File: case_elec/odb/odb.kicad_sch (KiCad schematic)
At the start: 9 parts, among them J1 Screw_Terminal_01x02, J2 Conn_02x07_Top_Bottom, SW1 SW_SPST, SW2 SW_SPST, U1 REYAX RYLR896, U2 BNO055, U3 MPL3115A, U4 Ultimate_GPS, U5 Teensy3.5

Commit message: amélioration route sw
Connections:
- net +5V: no longer SW2.2 (B)
- net at J1.1 (Pin_1), SW1.1 (A): now also SW2.2 (B)
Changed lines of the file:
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@@
   (junction (at 144.78 34.29) (diameter 0) (color 0 0 0 0)
   )
+  (junction (at 58.42 81.28) (diameter 0) (color 0 0 0 0)
+  )
   (junction (at 72.39 81.28) (diameter 0) (color 0 0 0 0)
   )
@@
     (stroke (width 0) (type default) (color 0 0 0 0))
   )
-  (wire (pts (xy 59.69 81.28) (xy 57.15 81.28))
+  (wire (pts (xy 59.69 81.28) (xy 58.42 81.28))
     (stroke (width 0) (type default) (color 0 0 0 0))
   )
@@
     (stroke (width 0) (type default) (color 0 0 0 0))
   )
-  (polyline (pts (xy 20.32 115.57) (xy 92.71 115.57))
+  (polyline (pts (xy 20.32 115.57) (xy 96.52 115.57))
     (stroke (width 0) (type default) (color 0 0 0 0))
   )
@@
     (stroke (width 0) (type default) (color 0 0 0 0))
   )
-  (polyline (pts (xy 92.71 115.57) (xy 92.71 152.4))
+  (polyline (pts (xy 96.52 115.57) (xy 96.52 152.4))
     (stroke (width 0) (type default) (color 0 0 0 0))
   )
@@
     (stroke (width 0) (type default) (color 0 0 0 0))
   )
-  (wire (pts (xy 77.47 142.24) (xy 95.25 142.24))
-    (stroke (width 0) (type default) (color 0 0 0 0))
-  )
   (wire (pts (xy 167.64 158.75) (xy 163.83 158.75))
     (stroke (width 0) (type default) (color 0 0 0 0))
@@
     (stroke (width 0) (type default) (color 0 0 0 0))
   )
+  (wire (pts (xy 58.42 81.28) (xy 58.42 113.03))
+    (stroke (width 0) (type default) (color 0 0 0 0))
+  )
   (wire (pts (xy 129.54 39.37) (xy 151.13 39.37))
     (stroke (width 0) (type default) (color 0 0 0 0))
   )
+  (wire (pts (xy 77.47 142.24) (xy 99.06 142.24))
+    (stroke (width 0) (type default) (color 0 0 0 0))
+  )
   (wire (pts (xy 107.95 83.82) (xy 99.06 83.82))
     (stroke (width 0) (type default) (color 0 0 0 0))
@@
     (stroke (width 0) (type default) (color 0 0 0 0))
   )
-  (wire (pts (xy 95.25 128.27) (xy 95.25 129.54))
-    (stroke (width 0) (type default) (color 0 0 0 0))
-  )
   (bus (pts (xy 170.18 171.45) (xy 170.18 168.91))
     (stroke (width 0) (type default) (color 0 0 0 0))
@@
     (stroke (width 0) (type default) (color 0 0 0 0))
   )
-  (polyline (pts (xy 92.71 152.4) (xy 20.32 152.4))
+  (polyline (pts (xy 96.52 152.4) (xy 20.32 152.4))
     (stroke (width 0) (type default) (color 0 0 0 0))
   )
@@
     (stroke (width 0) (type default) (color 0 0 0 0))
   )
-  (wire (pts (xy 91.44 129.54) (xy 95.25 129.54))
+  (wire (pts (xy 91.44 129.54) (xy 92.71 129.54))
     (stroke (width 0) (type default) (color 0 0 0 0))
   )
@@
     (stroke (width 0) (type default) (color 0 0 0 0))
   )
-  (wire (pts (xy 95.25 142.24) (xy 95.25 143.51))
+  (wire (pts (xy 99.06 142.24) (xy 99.06 143.51))
     (stroke (width 0) (type default) (color 0 0 0 0))
   )
@@
     (stroke (width 0) (type default) (color 0 0 0 0))
   )
+  (wire (pts (xy 58.42 81.28) (xy 57.15 81.28))
+    (stroke (width 0) (type default) (color 0 0 0 0))
+  )
   (wire (pts (xy 107.95 54.61) (xy 151.13 54.61))
     (stroke (width 0) (type default) (color 0 0 0 0))
@@
     (stroke (width 0) (type default) (color 0 0 0 0))
   )
+  (wire (pts (xy 58.42 113.03) (xy 92.71 113.03))
+    (stroke (width 0) (type default) (color 0 0 0 0))
+  )
   (wire (pts (xy 151.13 161.29) (xy 147.32 161.29))
     (stroke (width 0) (type default) (color 0 0 0 0))
@@
   )
   (wire (pts (xy 102.87 93.98) (xy 99.06 93.98))
+    (stroke (width 0) (type default) (color 0 0 0 0))
+  )
+  (wire (pts (xy 92.71 113.03) (xy 92.71 129.54))
     (stroke (width 0) (type default) (color 0 0 0 0))
   )
@@
     (pin "~")
   )
-  (symbol (lib_id "power:GND") (at 95.25 143.51 0) (unit 1)
-    (in_bom yes) (on_board yes)
-    (property "Reference" "#PWR04" (id 0) (at 95.25 149.86 0)
-      (effects (font (size 1.27 1.27)) hide)
-    )
-    (property "Value" "GND" (id 1) (at 95.25 148.59 0))
-    (property "Footprint" "" (id 2) (at 95.25 143.51 0)
-      (effects (font (size 1.27 1.27)) hide)
-    )
-    (property "Datasheet" "" (id 3) (at 95.25 143.51 0)
+  (symbol (lib_id "power:GND") (at 99.06 143.51 0) (unit 1)
+    (in_bom yes) (on_board yes)
+    (property "Reference" "#PWR04" (id 0) (at 99.06 149.86 0)
+      (effects (font (size 1.27 1.27)) hide)
+    )
+    (property "Value" "GND" (id 1) (at 99.06 148.59 0))
+    (property "Footprint" "" (id 2) (at 99.06 143.51 0)
+      (effects (font (size 1.27 1.27)) hide)
+    )
+    (property "Datasheet" "" (id 3) (at 99.06 143.51 0)
       (effects (font (size 1.27 1.27)) hide)
     )
@@
     (pin "6")
   )
-  (symbol (lib_id "power:+5V") (at 95.25 128.27 0) (unit 1)
-    (in_bom yes) (on_board yes)
-    (property "Reference" "#PWR03" (id 0) (at 95.25 132.08 0)
-      (effects (font (size 1.27 1.27)) hide)
-    )
-    (property "Value" "+5V" (id 1) (at 95.25 123.19 0))
-    (property "Footprint" "" (id 2) (at 95.25 128.27 0)
-      (effects (font (size 1.27 1.27)) hide)
-    )
-    (property "Datasheet" "" (id 3) (at 95.25 128.27 0)
-      (effects (font (size 1.27 1.27)) hide)
-    )
-    (pin "1")
-  )
   (symbol (lib_id "power:+5V") (at 72.39 82.55 180) (unit 1)
     (in_bom yes) (on_board yes) (fields_autoplaced)
@@
       (reference "#PWR02") (unit 1) (value "+5V") (footprint "")
     )
-    (path "/bacfcaea-5c0b-42ab-980e-cb8f47a6819e"
-      (reference "#PWR03") (unit 1) (value "+5V") (footprint "")
-    )
     (path "/7e28eb0b-eb99-4229-b4b8-2afb2f4b8e69"

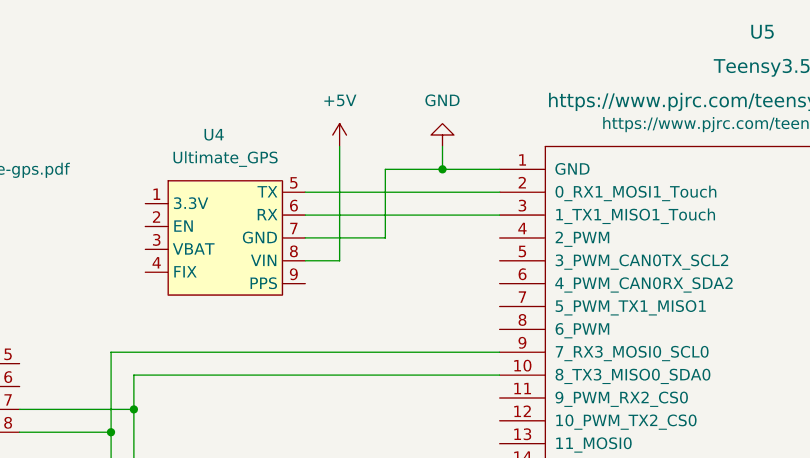
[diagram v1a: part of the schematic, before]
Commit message: Nouveau mapping perçage + gerber
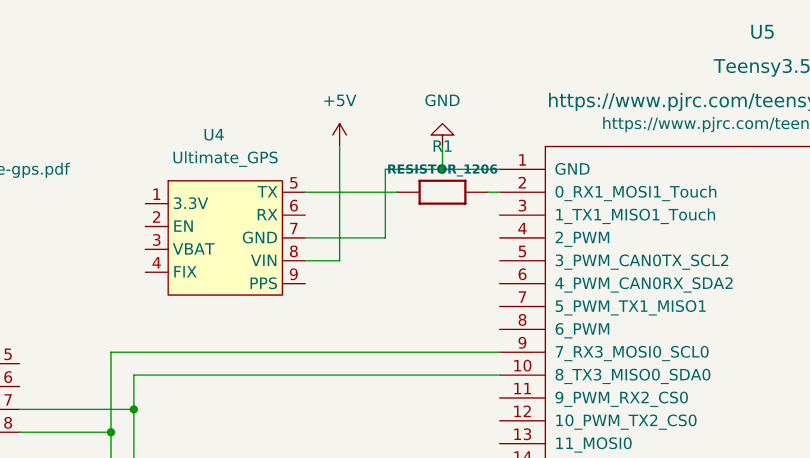
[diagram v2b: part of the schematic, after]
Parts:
- added R1: RESISTOR_1206, Resistor_SMD:R_1206_3216Metric_Pad1.30x1.75mm_HandSolder, symbol odb-eagle-import:RESISTOR_1206
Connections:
- net at U5.2 (0_RX1_MOSI1_Touch): now also R1.2; no longer U4.5 (TX)
- net at U5.3 (1_TX1_MISO1_Touch): no longer U4.6 (RX)
- new net: R1.1, U4.5 (TX)
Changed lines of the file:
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@@
+    (stroke (width 0) (type default) (color 0 0 0 0))
+  )
+  (wire (pts (xy 149.86 36.83) (xy 151.13 36.83))
+    (stroke (width 0) (type default) (color 0 0 0 0))
+  )
+  (wire (pts (xy 129.54 36.83) (xy 139.7 36.83))
     (stroke (width 0) (type default) (color 0 0 0 0))
   )
@@
     (stroke (width 0) (type default) (color 0 0 0 0))
   )
-  (wire (pts (xy 129.54 39.37) (xy 151.13 39.37))
-    (stroke (width 0) (type default) (color 0 0 0 0))
-  )
   (wire (pts (xy 77.47 142.24) (xy 99.06 142.24))
     (stroke (width 0) (type default) (color 0 0 0 0))
@@
   )
   (polyline (pts (xy 96.52 152.4) (xy 20.32 152.4))
-    (stroke (width 0) (type default) (color 0 0 0 0))
-  )
-  (wire (pts (xy 129.54 36.83) (xy 151.13 36.83))
     (stroke (width 0) (type default) (color 0 0 0 0))
   )
@@
     (pin "2")
   )
+  (symbol (lib_id "odb-eagle-import:RESISTOR_1206") (at 144.78 36.83 0) (unit 1)
+    (in_bom yes) (on_board yes) (fields_autoplaced)
+    (property "Reference" "R1" (id 0) (at 144.78 31.75 0))
+    (property "Value" "RESISTOR_1206" (id 1) (at 144.78 34.29 0)
+      (effects (font (size 1.016 1.016) bold))
+    )
+    (property "Footprint" "Resistor_SMD:R_1206_3216Metric_Pad1.30x1.75mm_HandSolder" (id 2) (at 144.78 36.83 0)
+      (effects (font (size 1.27 1.27)) hide)
+    )
+    (property "Datasheet" "" (id 3) (at 144.78 36.83 0)
+      (effects (font (size 1.27 1.27)) hide)
+    )
+    (pin "1")
+    (pin "2")
+  )
   (symbol (lib_id "reyax_rylr896:REYAX RYLR896") (at 59.69 135.89 0) (mirror y) (unit 1)
     (in_bom yes) (on_board yes)
@@
       (reference "J2") (unit 1) (value "Conn_02x07_Top_Bottom") (footprint "Connector_Molex:Molex_Nano-Fit_105310-xx14_2x07_P2.50mm_Vertical")
     )
+    (path "/92122d1f-5730-4015-aa36-a6febc7e4df1"
+      (reference "R1") (unit 1) (value "RESISTOR_1206") (footprint "Resistor_SMD:R_1206_3216Metric_Pad1.30x1.75mm_HandSolder")
+    )
     (path "/9077b56f-c102-47b4-9a60-c432e96c7e85"

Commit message: Suppression de la deuxième smd + modification sur le schema
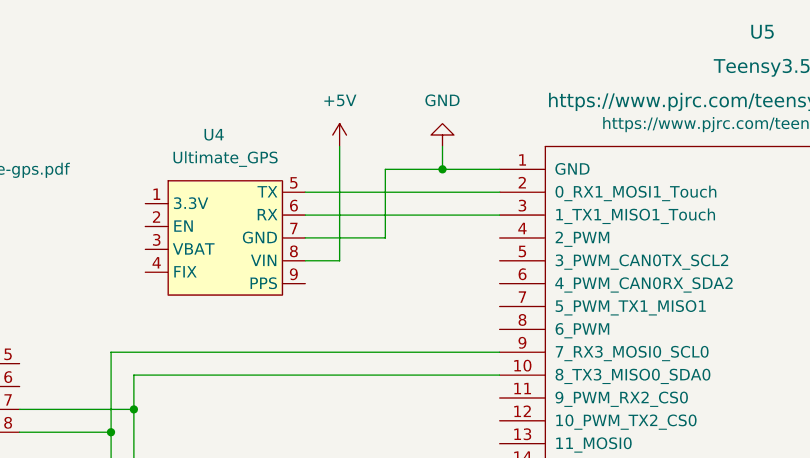
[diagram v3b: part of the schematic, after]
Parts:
- removed R1: RESISTOR_1206, Resistor_SMD:R_1206_3216Metric_Pad1.30x1.75mm_HandSolder, symbol odb-eagle-import:RESISTOR_1206
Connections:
- net at U5.2 (0_RX1_MOSI1_Touch): now also U4.5 (TX)
- net at U5.3 (1_TX1_MISO1_Touch): now also U4.6 (RX)
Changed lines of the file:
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@@
     (stroke (width 0) (type default) (color 0 0 0 0))
   )
-  (wire (pts (xy 149.86 36.83) (xy 151.13 36.83))
-    (stroke (width 0) (type default) (color 0 0 0 0))
-  )
-  (wire (pts (xy 129.54 36.83) (xy 139.7 36.83))
+  (wire (pts (xy 129.54 36.83) (xy 151.13 36.83))
     (stroke (width 0) (type default) (color 0 0 0 0))
   )
@@
   )
   (wire (pts (xy 58.42 81.28) (xy 58.42 113.03))
+    (stroke (width 0) (type default) (color 0 0 0 0))
+  )
+  (wire (pts (xy 129.54 39.37) (xy 151.13 39.37))
     (stroke (width 0) (type default) (color 0 0 0 0))
   )
@@
     (pin "2")
   )
-  (symbol (lib_id "odb-eagle-import:RESISTOR_1206") (at 144.78 36.83 0) (unit 1)
-    (in_bom yes) (on_board yes) (fields_autoplaced)
-    (property "Reference" "R1" (id 0) (at 144.78 31.75 0))
-    (property "Value" "RESISTOR_1206" (id 1) (at 144.78 34.29 0)
-      (effects (font (size 1.016 1.016) bold))
-    )
-    (property "Footprint" "Resistor_SMD:R_1206_3216Metric_Pad1.30x1.75mm_HandSolder" (id 2) (at 144.78 36.83 0)
-      (effects (font (size 1.27 1.27)) hide)
-    )
-    (property "Datasheet" "" (id 3) (at 144.78 36.83 0)
-      (effects (font (size 1.27 1.27)) hide)
-    )
-    (pin "1")
-    (pin "2")
-  )
   (symbol (lib_id "reyax_rylr896:REYAX RYLR896") (at 59.69 135.89 0) (mirror y) (unit 1)
     (in_bom yes) (on_board yes)
@@
       (reference "J2") (unit 1) (value "Conn_02x07_Top_Bottom") (footprint "Connector_Molex:Molex_Nano-Fit_105310-xx14_2x07_P2.50mm_Vertical")
     )
-    (path "/92122d1f-5730-4015-aa36-a6febc7e4df1"
-      (reference "R1") (unit 1) (value "RESISTOR_1206") (footprint "Resistor_SMD:R_1206_3216Metric_Pad1.30x1.75mm_HandSolder")
-    )
     (path "/9077b56f-c102-47b4-9a60-c432e96c7e85"

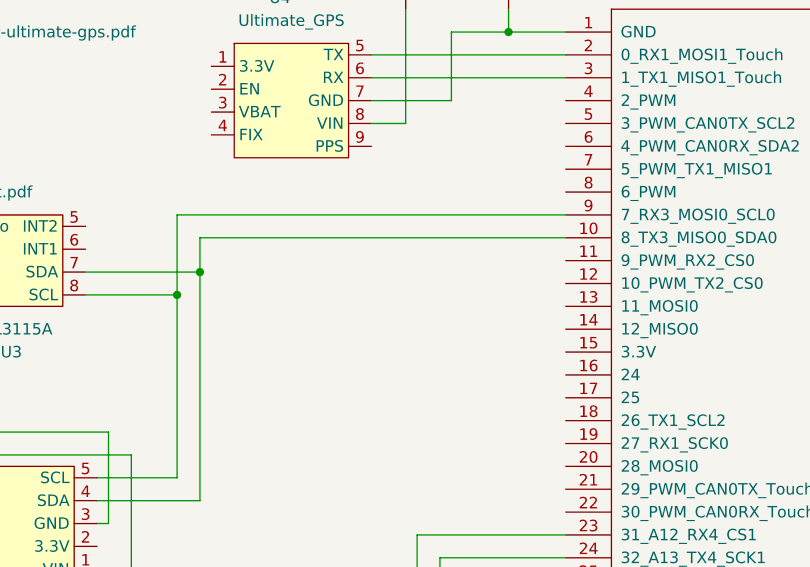
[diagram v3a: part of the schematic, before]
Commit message: Amélioration du code + fsm multitache
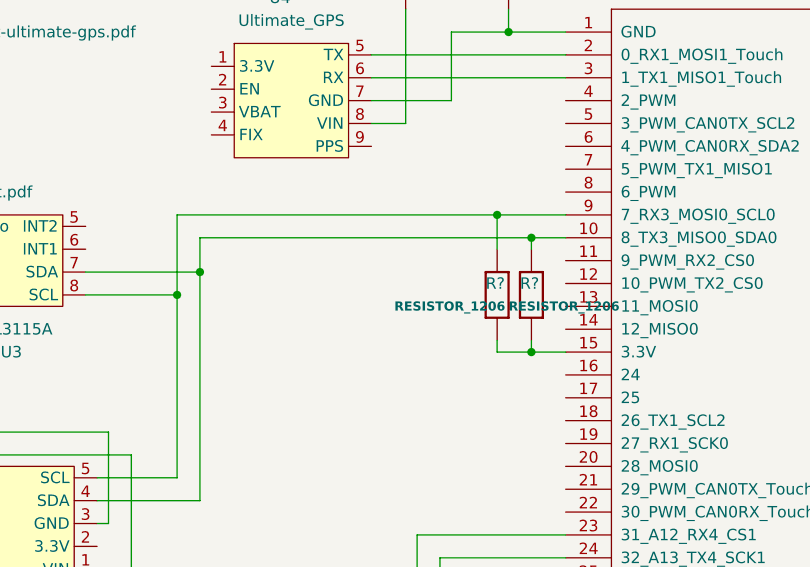
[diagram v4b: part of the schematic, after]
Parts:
- added R? (x2): RESISTOR_1206, odb:_1206, symbol odb-eagle-import:RESISTOR_1206
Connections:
- net at U2.4 (SDA), U3.7 (SDA), U5.10 (8_TX3_MISO0_SDA0): now also R?.2
- net at U2.5 (SCL), U3.8 (SCL), U5.9 (7_RX3_MOSI0_SCL0): now also R?.2
- net at U5.15 (3.3V): now also R?.1, R?.1
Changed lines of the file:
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@@
   (junction (at 76.2 78.74) (diameter 0) (color 0 0 0 0)
   )
+  (junction (at 147.32 69.85) (diameter 0) (color 0 0 0 0)
+  )
   (junction (at 170.18 153.67) (diameter 0) (color 0 0 0 0)
   )
@@
   (junction (at 58.42 81.28) (diameter 0) (color 0 0 0 0)
   )
+  (junction (at 147.32 57.15) (diameter 0) (color 0 0 0 0)
+  )
   (junction (at 72.39 81.28) (diameter 0) (color 0 0 0 0)
   )
@@
   (junction (at 110.49 60.96) (diameter 0) (color 0 0 0 0)
   )
+  (junction (at 143.51 54.61) (diameter 0) (color 0 0 0 0)
+  )
   (bus_entry (at 167.64 158.75) (size 2.54 -2.54)
     (stroke (width 0) (type default) (color 0 0 0 0))
@@
     (stroke (width 0) (type default) (color 0 0 0 0))
   )
+  (wire (pts (xy 143.51 69.85) (xy 147.32 69.85))
+    (stroke (width 0) (type default) (color 0 0 0 0))
+  )
   (wire (pts (xy 151.13 173.99) (xy 147.32 173.99))
     (stroke (width 0) (type default) (color 0 0 0 0))
@@
     (stroke (width 0) (type default) (color 0 0 0 0))
   )
+  (wire (pts (xy 143.51 68.58) (xy 143.51 69.85))
+    (stroke (width 0) (type default) (color 0 0 0 0))
+  )
   (wire (pts (xy 167.64 158.75) (xy 163.83 158.75))
     (stroke (width 0) (type default) (color 0 0 0 0))
@@
     (stroke (width 0) (type default) (color 0 0 0 0))
   )
+  (wire (pts (xy 147.32 68.58) (xy 147.32 69.85))
+    (stroke (width 0) (type default) (color 0 0 0 0))
+  )
   (bus (pts (xy 144.78 163.83) (xy 144.78 161.29))
     (stroke (width 0) (type default) (color 0 0 0 0))
@@
     (stroke (width 0) (type default) (color 0 0 0 0))
   )
+  (wire (pts (xy 147.32 69.85) (xy 151.13 69.85))
+    (stroke (width 0) (type default) (color 0 0 0 0))
+  )
   (wire (pts (xy 167.64 161.29) (xy 163.83 161.29))
     (stroke (width 0) (type default) (color 0 0 0 0))
@@
     (stroke (width 0) (type default) (color 0 0 0 0))
   )
+  (wire (pts (xy 147.32 57.15) (xy 151.13 57.15))
+    (stroke (width 0) (type default) (color 0 0 0 0))
+  )
   (wire (pts (xy 151.13 163.83) (xy 147.32 163.83))
     (stroke (width 0) (type default) (color 0 0 0 0))
@@
     (stroke (width 0) (type default) (color 0 0 0 0))
   )
-  (wire (pts (xy 107.95 54.61) (xy 151.13 54.61))
+  (wire (pts (xy 107.95 54.61) (xy 143.51 54.61))
     (stroke (width 0) (type default) (color 0 0 0 0))
   )
@@
     (stroke (width 0) (type default) (color 0 0 0 0))
   )
-  (wire (pts (xy 110.49 57.15) (xy 151.13 57.15))
+  (wire (pts (xy 110.49 57.15) (xy 147.32 57.15))
     (stroke (width 0) (type default) (color 0 0 0 0))
   )
@@
     (stroke (width 0) (type default) (color 0 0 0 0))
   )
+  (wire (pts (xy 143.51 54.61) (xy 143.51 58.42))
+    (stroke (width 0) (type default) (color 0 0 0 0))
+  )
   (wire (pts (xy 69.85 81.28) (xy 72.39 81.28))
     (stroke (width 0) (type default) (color 0 0 0 0))
@@
     (stroke (width 0) (type default) (color 0 0 0 0))
   )
+  (wire (pts (xy 143.51 54.61) (xy 151.13 54.61))
+    (stroke (width 0) (type default) (color 0 0 0 0))
+  )
   (wire (pts (xy 138.43 34.29) (xy 144.78 34.29))
     (stroke (width 0) (type default) (color 0 0 0 0))
@@
   )
   (bus (pts (xy 144.78 128.27) (xy 144.78 130.81))
+    (stroke (width 0) (type default) (color 0 0 0 0))
+  )
+  (wire (pts (xy 147.32 57.15) (xy 147.32 58.42))
     (stroke (width 0) (type default) (color 0 0 0 0))
   )
@@
     )
     (pin "1")
+  )
+  (symbol (lib_id "odb-eagle-import:RESISTOR_1206") (at 143.51 63.5 90) (unit 1)
+    (in_bom yes) (on_board yes)
+    (property "Reference" "R?" (id 0) (at 142.24 62.23 90)
+      (effects (font (size 1.27 1.27)) (justify right))
+    )
+    (property "Value" "RESISTOR_1206" (id 1) (at 132.08 64.77 90)
+      (effects (font (size 1.016 1.016) bold) (justify right))
+    )
+    (property "Footprint" "odb:_1206" (id 2) (at 143.51 63.5 0)
+      (effects (font (size 1.27 1.27)) hide)
+    )
+    (property "Datasheet" "" (id 3) (at 143.51 63.5 0)
+      (effects (font (size 1.27 1.27)) hide)
+    )
+    (pin "1")
+    (pin "2")
   )
   (symbol (lib_id "power:GND") (at 144.78 31.75 180) (unit 1)
@@
     (pin "6")
   )
+  (symbol (lib_id "odb-eagle-import:RESISTOR_1206") (at 147.32 63.5 90) (unit 1)
+    (in_bom yes) (on_board yes)
+    (property "Reference" "R?" (id 0) (at 146.05 62.23 90)
+      (effects (font (size 1.27 1.27)) (justify right))
+    )
+    (property "Value" "RESISTOR_1206" (id 1) (at 144.78 64.77 90)
+      (effects (font (size 1.016 1.016) bold) (justify right))
+    )
+    (property "Footprint" "odb:_1206" (id 2) (at 147.32 63.5 0)
+      (effects (font (size 1.27 1.27)) hide)
+    )
+    (property "Datasheet" "" (id 3) (at 147.32 63.5 0)
+      (effects (font (size 1.27 1.27)) hide)
+    )
+    (pin "1")
+    (pin "2")
+  )
   (symbol (lib_id "power:+5V") (at 72.39 82.55 180) (unit 1)
     (in_bom yes) (on_board yes) (fields_autoplaced)
@@
       (reference "J2") (unit 1) (value "Conn_02x07_Top_Bottom") (footprint "Connector_Molex:Molex_Nano-Fit_105310-xx14_2x07_P2.50mm_Vertical")
     )
+    (path "/4e8e4de4-d9e4-4608-8075-d2f314dddb32"
+      (reference "R?") (unit 1) (value "RESISTOR_1206") (footprint "odb:_1206")
+    )
+    (path "/ad6e206d-e388-450b-b6a7-2adb10012459"
+      (reference "R?") (unit 1) (value "RESISTOR_1206") (footprint "odb:_1206")
+    )
     (path "/9077b56f-c102-47b4-9a60-c432e96c7e85"
